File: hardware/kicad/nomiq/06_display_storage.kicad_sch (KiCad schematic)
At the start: 12 parts, among them J7 TFT 2.4in ILI9341 SPI FPC, J8 microSD push-push, Q1 AO3400A

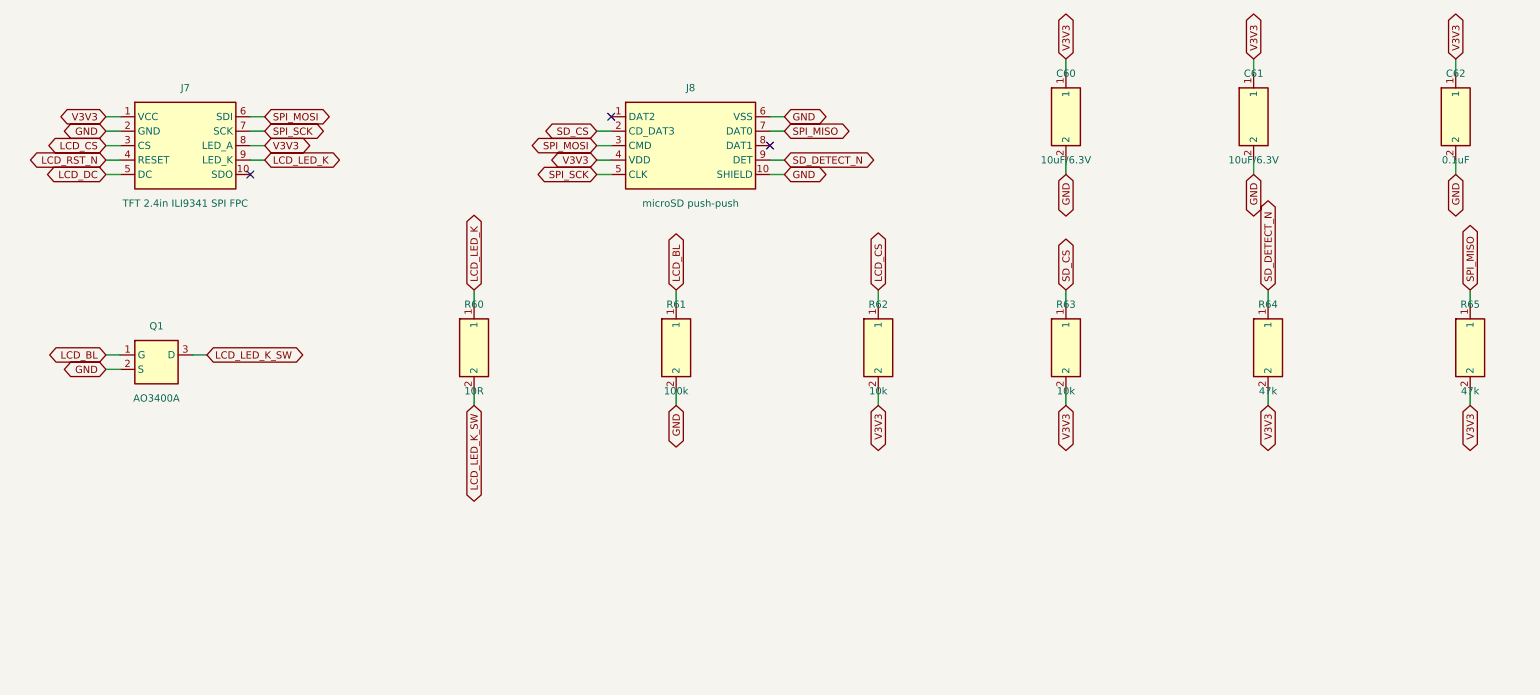
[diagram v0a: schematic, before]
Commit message: feat(sch): verified pad maps and project footprint library for all 138 parts
- fplib.py: 36 footprints from the KiCad library / Espressif library (+ TFT module),
  written to lib/nomiq.pretty and checked (make tools)
- nomiq_hw.py: per-part datasheet pin->pad maps; gen_kicad checks every pad exists
  and every copper pad is mapped (0 unverified parts)
- TPS63802 -> TPS63001 (fixed 3.3 V, KiCad DRC land pattern); BQ24074 RILIM/ITERM/TMR
  corrected to datasheet constants; TCXO 1.8 V (E) variant to match DIO3 setting
- RF blocks expanded into discrete choke, 2-section low-pass, lattice balun, DC blocks
  (PE4259 ports must be DC-free) and DNP pi tuning pads
- Display: 14-pin ILI9341 module, high-side P-FET backlight switch; microSD detect pins,
  connector mounting pads, MAX98357A NC pads

REQ-PCB-001, REQ-PCB-007

Co-Authored-By: Claude Opus 5.5 <noreply@anthropic.com>
Claude-Session: https://claude.ai/code/session_01HafD3UN2tDPG8DjCdm2PVK
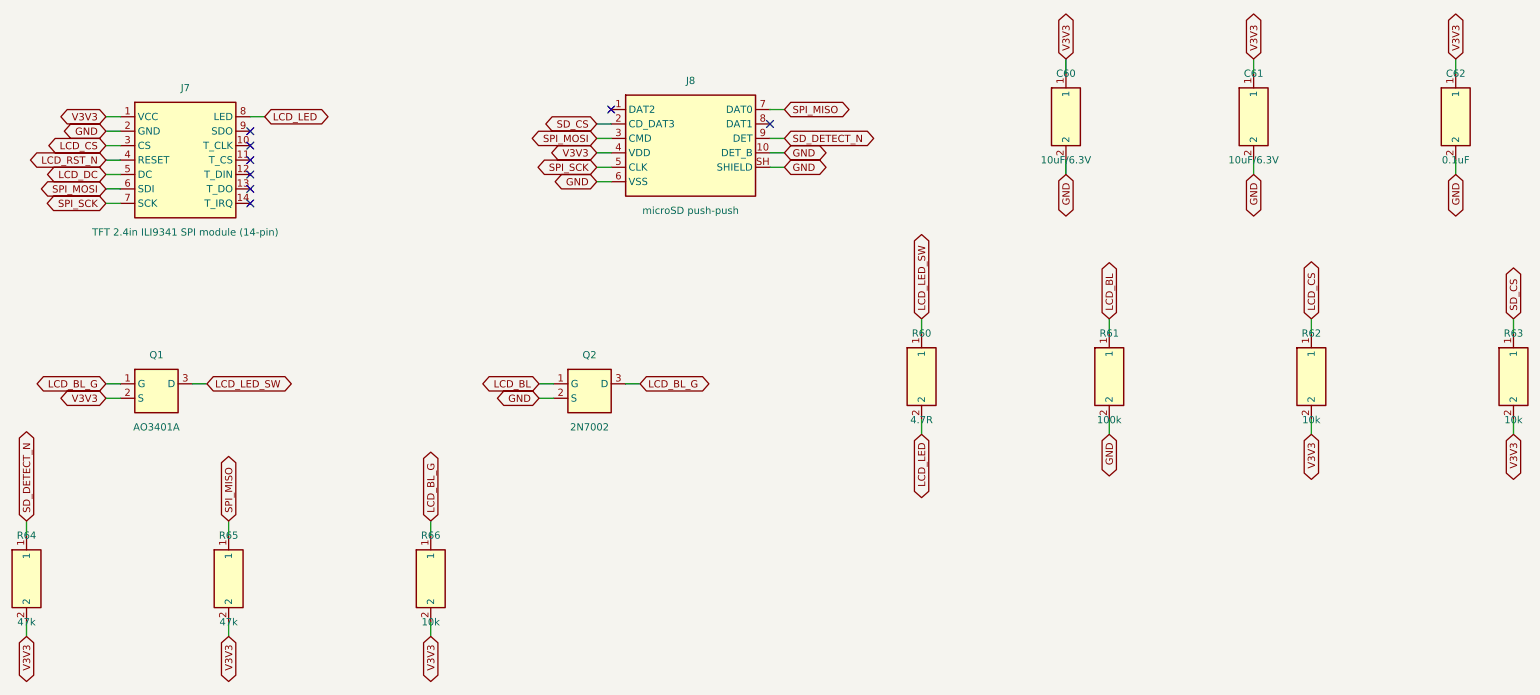
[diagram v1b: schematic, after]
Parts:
- added Q2: 2N7002, nomiq:SOT-23, symbol nomiq:Q2_2N7002
- added R66: 10k, nomiq:R_0402_1005Metric, symbol nomiq:R66_10k
- C60, C61: footprint Capacitor_SMD:C_0603_1608Metric -> nomiq:C_0603_1608Metric
- C62: footprint Capacitor_SMD:C_0402_1005Metric -> nomiq:C_0402_1005Metric
- J7: value TFT 2.4in ILI9341 SPI FPC -> TFT 2.4in ILI9341 SPI module (14-pin); footprint (none) -> nomiq:TFT_2.4in_ILI9341_1x14; symbol nomiq:J7_TFT_2_4in_ILI9341_SPI_FP -> nomiq:J7_TFT_2_4in_ILI9341_SPI_mo; MPN module-specific -> 2.4in 240x320 ILI9341 SPI module, 1x14 2.54 mm; PadMap unverified -> datasheet
- J8: footprint Connector_Card:microSD_HC_Molex_104031-0811 -> nomiq:microSD_HC_Molex_104031-0811; PadMap unverified -> datasheet; Verify yes -> (none)
- Q1: value AO3400A -> AO3401A; footprint Package_TO_SOT_SMD:SOT-23 -> nomiq:SOT-23; symbol nomiq:Q1_AO3400A -> nomiq:Q1_AO3401A; MPN AOS AO3400A -> AOS AO3401A; PadMap unverified -> datasheet
- R60: value 10R -> 4.7R; footprint Resistor_SMD:R_0402_1005Metric -> nomiq:R_0402_1005Metric; symbol nomiq:R60_10R -> nomiq:R60_4_7R
- R61, R62, R63, R64, R65: footprint Resistor_SMD:R_0402_1005Metric -> nomiq:R_0402_1005Metric
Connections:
- net GND: now also J8.SH (SHIELD), Q2.2 (S); no longer Q1.2 (S)
- net LCD_BL: now also Q2.1 (G); no longer Q1.1 (G)
- net V3V3: now also Q1.2 (S), R66.2; no longer J7.8 (LED_A)
- net LCD_LED_K: no longer names the net of J7.9 (SDO)
- net LCD_LED_K: no longer R60.1
- net LCD_LED_K_SW renamed LCD_LED
- net LCD_LED: now also J7.8 (LED); no longer Q1.3 (D)
- new net LCD_BL_G: Q1.1 (G), Q2.3 (D), R66.1
- new net LCD_LED_SW: Q1.3 (D), R60.1
- no-connect marks 3 -> 8
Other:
- moved on the sheet: Q1, R60, R61, R62, R63, R64, R65
